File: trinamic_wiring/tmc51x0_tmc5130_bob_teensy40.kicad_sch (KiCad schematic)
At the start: 4 parts, among them M1 Stepper_Motor

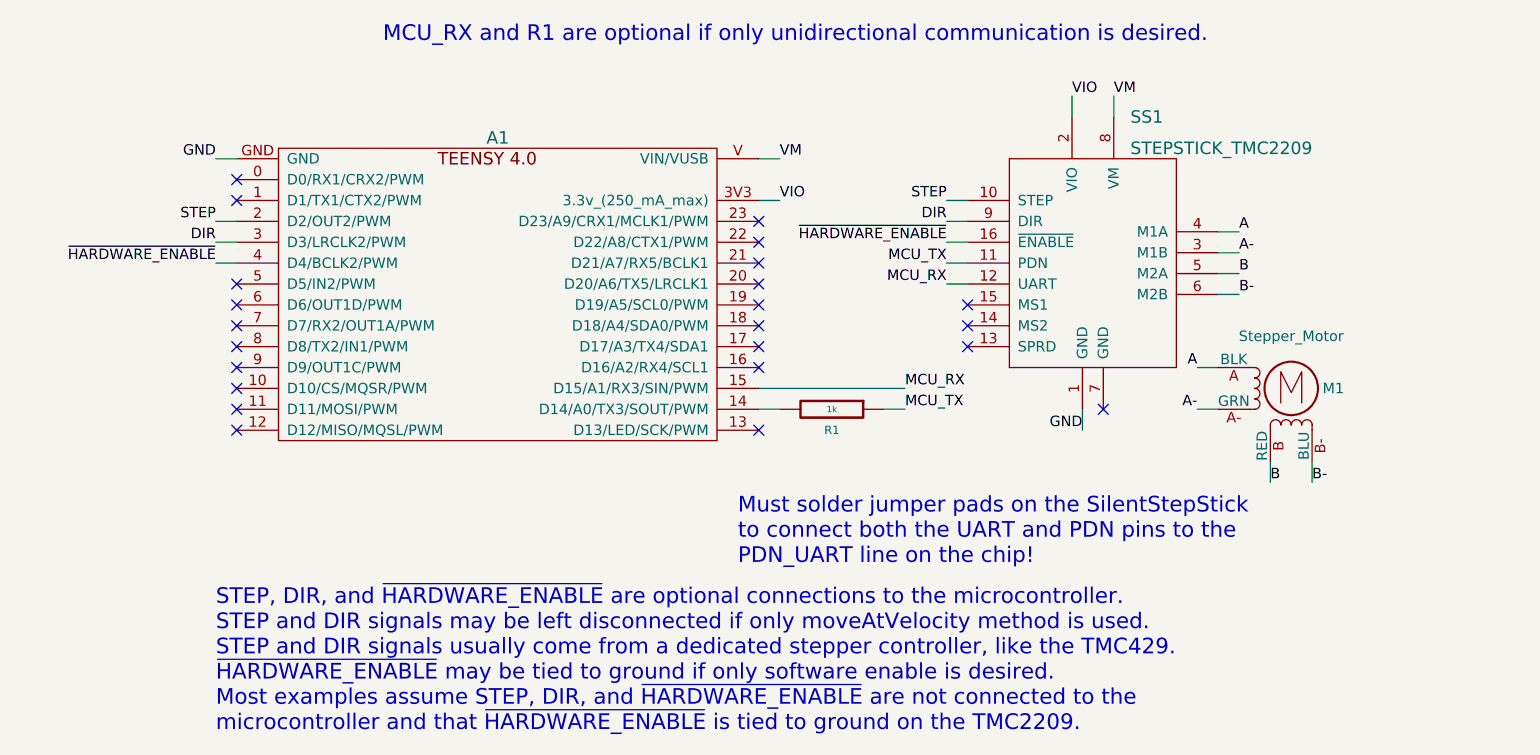
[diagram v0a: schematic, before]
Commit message: Remove unused sheets
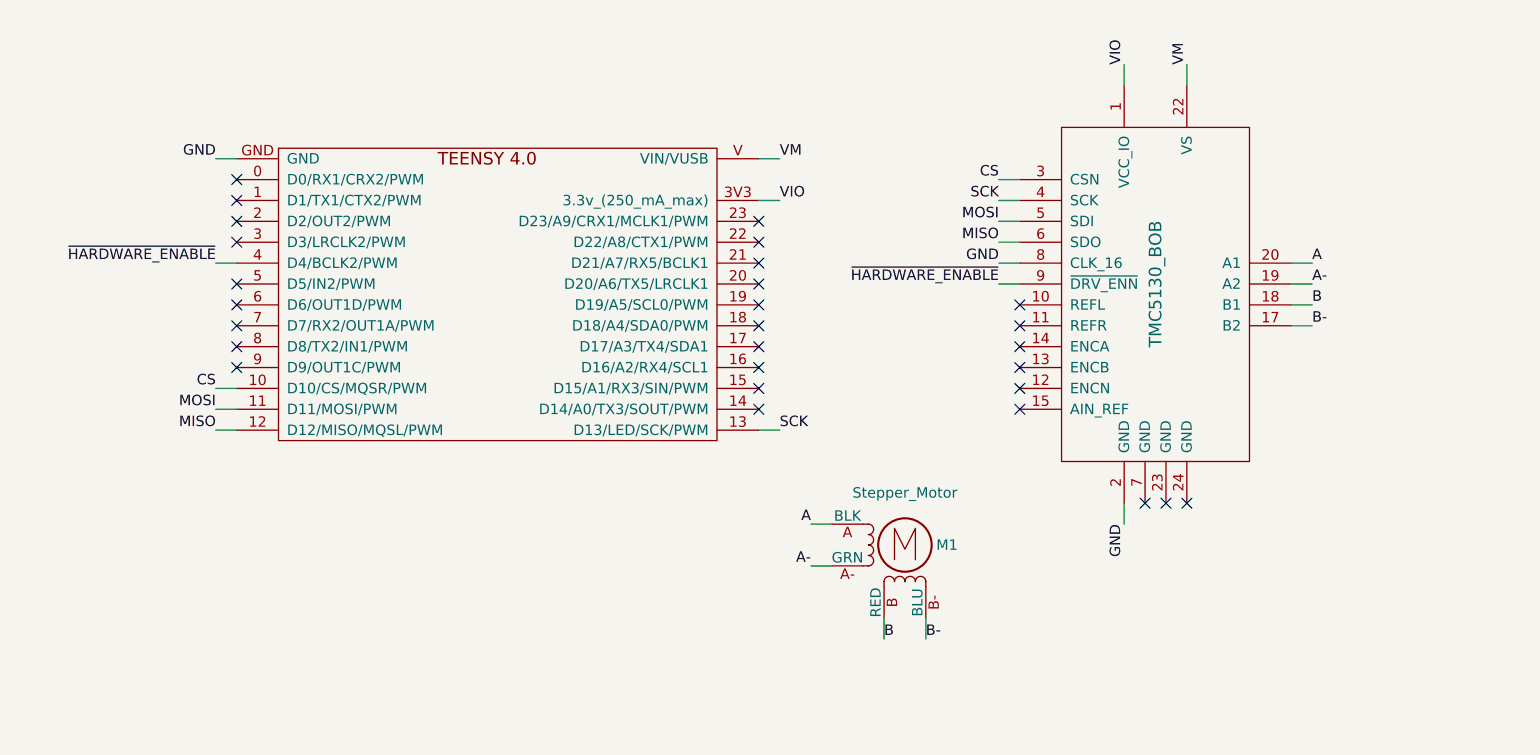
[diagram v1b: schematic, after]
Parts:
- removed R1: 1k, footprints:SM0805, symbol Janelia:1k_0805
- removed SS1: STEPSTICK_TMC2209, footprints:STEPSTICK_TMC2209, symbol Janelia:STEPSTICK_TMC2209
- added BOB1: TMC5130_BOB, symbol Janelia:TMC5130_BOB
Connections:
- net A: now also BOB1.20 (A1)
- net A-: now also BOB1.19 (A2)
- net B: now also BOB1.18 (B1)
- net B-: now also BOB1.17 (B2)
- net GND: now also BOB1.2 (GND), BOB1.8 (CLK_16)
- net VIO: now also BOB1.1 (VCC_IO)
- net VM: now also BOB1.22 (VS)
- net ~{HARDWARE_ENABLE}: now also BOB1.9 (~{DRV_ENN})
- net CS: now reaches A1.10 (D10/CS/MQSR/PWM)
- net CS: now also BOB1.3 (CSN)
- net MOSI: now reaches A1.11 (D11/MOSI/PWM)
- net MOSI: now also BOB1.5 (SDI)
- net MISO: now reaches A1.12 (D12/MISO/MQSL/PWM)
- net MISO: now also BOB1.6 (SDO)
- net SCK: now reaches A1.13 (D13/LED/SCK/PWM)
- net SCK: now also BOB1.4 (SCK)
- net DIR: no longer names the net of A1.3 (D3/LRCLK2/PWM)
- net MCU_RX: no longer names the net of A1.15 (D15/A1/RX3/SIN/PWM)
- net STEP: no longer names the net of A1.2 (D2/OUT2/PWM)
- no-connect marks 23 -> 28
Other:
- note removed: "MCU_RX and R1 are optional if only unidirectional communication is desired."
- note removed: "Must solder jumper pads on the SilentStepStick to connect both the UART and PDN pins to the PDN_UART line on the chip!"
- note removed: "STEP, DIR, and ~{HARDWARE_ENABLE} are optional connections to the microcontroller. STEP and DIR signals may be left disconnected if only moveAtVelocity method is used. STEP and DIR signals usually come from a dedicated stepper controller, like the TMC429. ~{HARDWARE_ENABLE} may be tied to ground if only software enable is desired. Most examples assume STEP, DIR, and ~{HARDWARE_ENABLE} are not con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"
- moved on the sheet: M1
